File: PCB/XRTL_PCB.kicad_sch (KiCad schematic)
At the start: 20 parts, among them J2 stepper1, J3 stepper2, K1 TIANBO-HJR-4102-L, K2 TIANBO-HJR-4102-L, U1 TBD62003, U2 TBD62003

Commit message: Add files via upload
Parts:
- D1: value (none) -> 1N4001; footprint (none) -> Diode_THT:D_DO-41_SOD81_P10.16mm_Horizontal
- J1: value (none) -> POWER; footprint (none) -> Connector_USB:USB_A_Stewart_SS-52100-001_Horizontal
- J10: value (none) -> servo1; footprint (none) -> Connector_PinHeader_2.54mm:PinHeader_1x03_P2.54mm_Horizontal
- J11: value (none) -> servo2; footprint (none) -> Connector_PinHeader_2.54mm:PinHeader_1x03_P2.54mm_Horizontal
- J12: value (none) -> infoLED; footprint (none) -> Connector_PinHeader_2.54mm:PinHeader_1x03_P2.54mm_Horizontal
- J4: value (none) -> ESP32 right; footprint (none) -> Connector_PinSocket_2.54mm:PinSocket_1x19_P2.54mm_Vertical
- J5: value (none) -> ESP32 left; footprint (none) -> Connector_PinSocket_2.54mm:PinSocket_1x19_P2.54mm_Vertical
- J6, J7, J9: footprint (none) -> TerminalBlock_Phoenix:TerminalBlock_Phoenix_MKDS-1,5-2-5.08_1x02_P5.08mm_Horizontal
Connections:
- net driverRelay1: now also D2.2 (A), K1.8, U2.10 (O7); no longer D1.2 (A), K2.8, U2.16 (O1)
- net driverRelay2: now also D1.2 (A), K2.8, U2.11 (O6); no longer D2.2 (A), K1.8, U2.15 (O2)
- net relay1: now also U2.7 (I7); no longer U2.1 (I1)
- net relay2: now also U2.6 (I6); no longer U2.2 (I2)
- net stepper1A: now also J5.8 (Pin_8), U1.7 (I7); no longer J5.2 (Pin_2), U1.4 (I4)
- net stepper1B: now also J5.6 (Pin_6), U1.6 (I6); no longer J5.3 (Pin_3), U1.3 (I3)
- net stepper1C: now also J5.3 (Pin_3), U1.5 (I5); no longer J5.6 (Pin_6), U1.2 (I2)
- net stepper1D: now also J5.2 (Pin_2), U1.4 (I4); no longer J5.8 (Pin_8), U1.1 (I1)
- net stepper2A: now also J5.12 (Pin_12), U2.4 (I4); no longer J5.9 (Pin_9), U2.7 (I7)
- net stepper2B: now also J5.11 (Pin_11), U2.3 (I3); no longer J5.10 (Pin_10), U2.6 (I6)
- net stepper2C: now also J5.10 (Pin_10), U2.2 (I2); no longer J5.11 (Pin_11), U2.5 (I5)
- net stepper2D: now also J5.9 (Pin_9), U2.1 (I1); no longer J5.12 (Pin_12), U2.4 (I4)
- net at J3.1 (Pin_1): now also U2.13 (O4); no longer U2.10 (O7)
- net at J3.2 (Pin_2): now also U2.14 (O3); no longer U2.11 (O6)
- net at U2.12 (O5): no longer J3.3 (Pin_3)
- net at J3.4 (Pin_4): now also U2.16 (O1); no longer U2.13 (O4)
- net at J2.1 (Pin_1): now also U1.10 (O7); no longer U1.13 (O4)
- net at J2.2 (Pin_2): now also U1.11 (O6); no longer U1.14 (O3)
- net at J2.3 (Pin_3): now also U1.12 (O5); no longer U1.15 (O2)
- net at J2.4 (Pin_4): now also U1.13 (O4); no longer U1.16 (O1)
- new net: J3.3 (Pin_3), U2.15 (O2)
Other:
- moved on the sheet: J2, J3

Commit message: Add files via upload
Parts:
- removed J1: POWER, Connector_USB:USB_A_Stewart_SS-52100-001_Horizontal, symbol Connector:USB_B
- added C3: 100n, Capacitor_THT:C_Disc_D3.0mm_W1.6mm_P2.50mm, symbol Device:C
- added J13: USBC_5V_3A_input, Connector_USB:USB_C_Receptacle_GCT_USB4085, symbol Connector:USB_C_Receptacle_USB2.0
- added R1, R2: 5.1k, Resistor_THT:R_Axial_DIN0204_L3.6mm_D1.6mm_P5.08mm_Horizontal, symbol Device:R_Small
- C1, C2: footprint Capacitor_THT:C_Disc_D3.4mm_W2.1mm_P2.50mm -> Capacitor_THT:C_Disc_D3.0mm_W1.6mm_P2.50mm
- J6: value (none) -> relay2 IN
- J7: value (none) -> relay1 IN
- J8: value (none) -> relay2 OUT; footprint (none) -> TerminalBlock_Phoenix:TerminalBlock_Phoenix_MKDS-1,5-2-5.08_1x02_P5.08mm_Horizontal
- J9: value (none) -> relay1 OUT
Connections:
- net +5V: now also C3.1, J13.A4 (VBUS), J13.A9 (VBUS), J13.B4 (VBUS), J13.B9 (VBUS)
- net GND: now also C3.2, J13.A1 (GND), J13.A12 (GND), J13.B1 (GND), J13.B12 (GND), J13.S1 (SHIELD), R1.2, R2.2
- net driverRelay1: now also U2.11 (O6); no longer U2.10 (O7)
- net driverRelay2: now also U2.10 (O7); no longer U2.11 (O6)
- net relay1: now also J4.11 (Pin_11); no longer J4.15 (Pin_15)
- new net: J13.A5 (CC1), R2.1
- new net: J13.B5 (CC2), R1.1
- no-connect marks 33 -> 36
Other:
- note added: "3V PWM w/o levelshifting verified for MG90S"
- note added: "5V 3A"
- note added: "LEDs ommited for final layout (intended for optics lab)"
- note added: "USB-C power connector"
- note added: "for "real" USB-C: sink is identified by 5.1k pull down on CC cable can be flipped => required on both CC1 and CC2"
- title: (none) -> XR Twin Lab
- moved on the sheet: C1, C2, D1, D2, J10, J11, J12, J2, J3, J4, J5, J6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

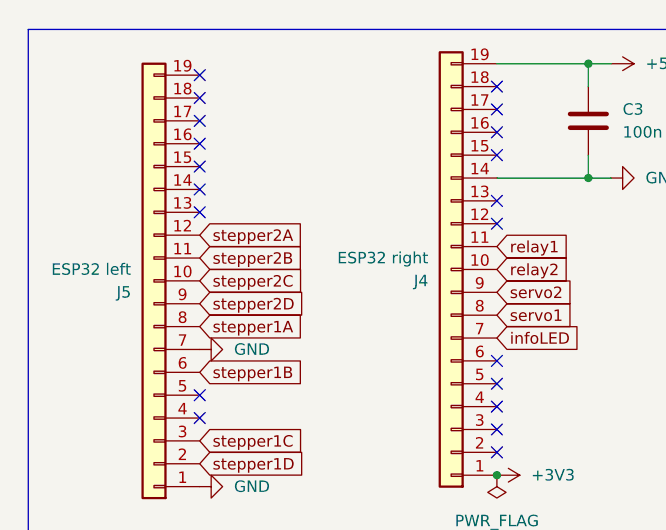
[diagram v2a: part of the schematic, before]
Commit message: Add files via upload
fixed pin assignment
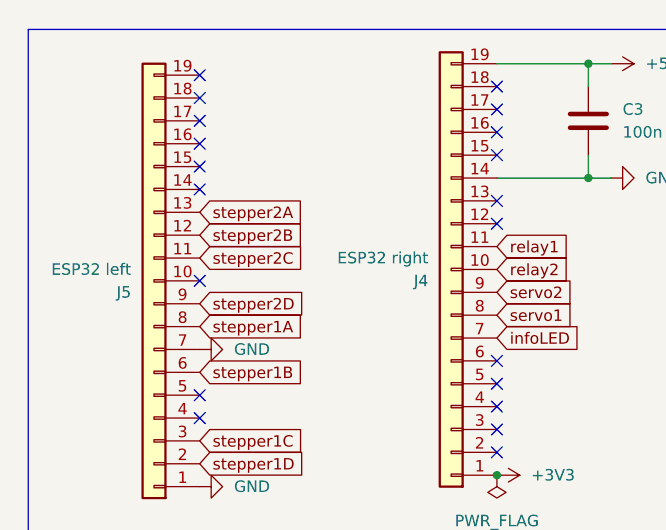
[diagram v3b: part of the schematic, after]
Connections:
- net stepper2A: now also J5.13 (Pin_13); no longer J5.12 (Pin_12)
- net stepper2B: now also J5.12 (Pin_12); no longer J5.11 (Pin_11)
- net stepper2C: now also J5.11 (Pin_11); no longer J5.10 (Pin_10)
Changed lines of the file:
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@@
   (no_connect (at 58.42 177.8))
   (no_connect (at 58.42 162.56))
-  (no_connect (at 33.02 35.56))
   (no_connect (at 66.04 34.29))
   (no_connect (at 66.04 21.59))
@@
   (no_connect (at 147.32 52.07))
   (no_connect (at 33.02 55.88))
+  (no_connect (at 33.02 43.18))
   (no_connect (at 66.04 26.67))
   (no_connect (at 58.42 175.26))
@@
     )
   )
-  (global_label "stepper2A" (shape input) (at 33.02 38.1 0) (fields_autoplaced)
-    (effects (font (size 1.27 1.27)) (justify left))
-    (property "Intersheet References" "${INTERSHEET_REFS}" (id 0) (at 44.7464 38.0206 0)
+  (global_label "stepper2A" (shape input) (at 33.02 35.56 0) (fields_autoplaced)
+    (effects (font (size 1.27 1.27)) (justify left))
+    (property "Intersheet References" "${INTERSHEET_REFS}" (id 0) (at 44.7464 35.4806 0)
       (effects (font (size 1.27 1.27)) (justify left) hide)
     )
@@
     )
   )
-  (global_label "stepper2C" (shape input) (at 33.02 43.18 0) (fields_autoplaced)
-    (effects (font (size 1.27 1.27)) (justify left))
-    (property "Intersheet References" "${INTERSHEET_REFS}" (id 0) (at 44.9279 43.1006 0)
+  (global_label "stepper2C" (shape input) (at 33.02 40.64 0) (fields_autoplaced)
+    (effects (font (size 1.27 1.27)) (justify left))
+    (property "Intersheet References" "${INTERSHEET_REFS}" (id 0) (at 44.9279 40.5606 0)
       (effects (font (size 1.27 1.27)) (justify left) hide)
     )
@@
     )
   )
-  (global_label "stepper2B" (shape input) (at 33.02 40.64 0) (fields_autoplaced)
-    (effects (font (size 1.27 1.27)) (justify left))
-    (property "Intersheet References" "${INTERSHEET_REFS}" (id 0) (at 44.9279 40.5606 0)
-      (effects (font (size 1.27 1.27)) (justify left) hide)
-    )
+  (global_label "stepper2B" (shape input) (at 33.02 38.1 0) (fields_autoplaced)
+    (effects (font (size 1.27 1.27)) (justify left))
+    (property "Intersheet References" "${INTERSHEET_REFS}" (id 0) (at 44.9279 38.0206 0)
+      (effects (font (size 1.27 1.27)) (justify left) hide)
+    )
